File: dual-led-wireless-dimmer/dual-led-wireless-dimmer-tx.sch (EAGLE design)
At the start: 43 parts, among them IC1 LM2937IMP-3.3, Q1 DN2625K4-G, Q2 SI2323DS-T1-E3, Q3 IRF520NPBF, Q4 IRF520NPBF, U1 ATMEGA328P_TQFP

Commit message: wip
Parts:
- added R12, R13: 150, microbuilder:RESISTOR0805
- Q3, Q4: value IRF520NPBF -> IRL520
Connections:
- new net N$1: Q3.G, R12.2
- new net N$2: Q4.G, R13.2
- net PWM1: now also R12.1; no longer Q3.G
- net PWM2: now also R13.1; no longer Q4.G
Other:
- moved on the sheet: OUT1-1, OUT1-2, OUT2-1, OUT2-2, Q3, Q4
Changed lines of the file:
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@@
 <?xml version="1.0" encoding="utf-8"?>
 <!DOCTYPE eagle SYSTEM "eagle.dtd">
-<eagle version="8.5.0">
+<eagle version="8.5.1">
 <drawing>
 <settings>
@@
 <part name="3.3V7" library="microbuilder" deviceset="3.3V" device=""/>
 <part name="12V1" library="microbuilder" deviceset="12V" device=""/>
-<part name="Q3" library="Seeed-Transistor-2016" deviceset="DIP-MOSFET-N-CH-100V-9.7A-IRF520NPBF(TO-220AB)" device="" value="IRF520NPBF"/>
+<part name="Q3" library="Seeed-Transistor-2016" deviceset="DIP-MOSFET-N-CH-100V-9.7A-IRF520NPBF(TO-220AB)" device="" value="IRL520"/>
 <part name="OUT1" library="con-ptr500" library_urn="urn:adsk.eagle:library:181" deviceset="AK550/2" device="" package3d_urn="urn:adsk.eagle:package:9907/1"/>
 <part name="12V2" library="microbuilder" deviceset="12V" device=""/>
@@
 <part name="R10" library="microbuilder" deviceset="RESISTOR" device="0805" value="10k"/>
 <part name="GND16" library="microbuilder" deviceset="GND" device=""/>
-<part name="Q4" library="Seeed-Transistor-2016" deviceset="DIP-MOSFET-N-CH-100V-9.7A-IRF520NPBF(TO-220AB)" device="" value="IRF520NPBF"/>
+<part name="Q4" library="Seeed-Transistor-2016" deviceset="DIP-MOSFET-N-CH-100V-9.7A-IRF520NPBF(TO-220AB)" device="" value="IRL520"/>
 <part name="OUT2" library="con-ptr500" library_urn="urn:adsk.eagle:library:181" deviceset="AK550/2" device="" package3d_urn="urn:adsk.eagle:package:9907/1"/>
 <part name="12V3" library="microbuilder" deviceset="12V" device=""/>
@@
 <part name="SJ3" library="SparkFun-Retired" deviceset="SOLDERJUMPER" device="NO"/>
 <part name="SJ1" library="SparkFun-Retired" deviceset="SOLDERJUMPER" device="NO"/>
+<part name="R12" library="microbuilder" deviceset="RESISTOR" device="0805" value="150"/>
+<part name="R13" library="microbuilder" deviceset="RESISTOR" device="0805" value="150"/>
 </parts>
 <sheets>
@@
 <instance part="3.3V7" gate="G$1" x="149.86" y="137.16" rot="R180"/>
 <instance part="12V1" gate="G$1" x="91.44" y="10.16"/>
-<instance part="Q3" gate="G$1" x="248.92" y="99.06"/>
-<instance part="OUT1" gate="-1" x="254" y="106.68" rot="R180"/>
-<instance part="OUT1" gate="-2" x="254" y="111.76" rot="R180"/>
-<instance part="12V2" gate="G$1" x="248.92" y="119.38"/>
-<instance part="GND18" gate="G$1" x="248.92" y="88.9"/>
+<instance part="Q3" gate="G$1" x="266.7" y="99.06"/>
+<instance part="OUT1" gate="-1" x="271.78" y="106.68" rot="R180"/>
+<instance part="OUT1" gate="-2" x="271.78" y="111.76" rot="R180"/>
+<instance part="12V2" gate="G$1" x="266.7" y="119.38"/>
+<instance part="GND18" gate="G$1" x="266.7" y="88.9"/>
 <instance part="R10" gate="G$1" x="238.76" y="93.98" rot="R270"/>
 <instance part="GND16" gate="G$1" x="238.76" y="86.36"/>
-<instance part="Q4" gate="G$1" x="248.92" y="60.96"/>
-<instance part="OUT2" gate="-1" x="254" y="68.58" rot="R180"/>
-<instance part="OUT2" gate="-2" x="254" y="73.66" rot="R180"/>
-<instance part="12V3" gate="G$1" x="248.92" y="81.28"/>
-<instance part="GND19" gate="G$1" x="248.92" y="50.8"/>
+<instance part="Q4" gate="G$1" x="266.7" y="60.96"/>
+<instance part="OUT2" gate="-1" x="271.78" y="68.58" rot="R180"/>
+<instance part="OUT2" gate="-2" x="271.78" y="73.66" rot="R180"/>
+<instance part="12V3" gate="G$1" x="266.7" y="81.28"/>
+<instance part="GND19" gate="G$1" x="266.7" y="50.8"/>
 <instance part="R11" gate="G$1" x="238.76" y="55.88" rot="R270"/>
 <instance part="GND17" gate="G$1" x="238.76" y="48.26"/>
@@
 <instance part="SJ3" gate="1" x="198.12" y="111.76"/>
 <instance part="SJ1" gate="1" x="198.12" y="116.84"/>
+<instance part="R12" gate="G$1" x="251.46" y="99.06"/>
+<instance part="R13" gate="G$1" x="251.46" y="60.96"/>
 </instances>
 <busses>
@@
 <pinref part="Q3" gate="G$1" pin="S"/>
 <pinref part="GND18" gate="G$1" pin="GND"/>
-<wire x1="248.92" y1="91.44" x2="248.92" y2="93.98" width="0.1524" layer="91"/>
+<wire x1="266.7" y1="91.44" x2="266.7" y2="93.98" width="0.1524" layer="91"/>
 </segment>
 <segment>
@@
 <pinref part="Q4" gate="G$1" pin="S"/>
 <pinref part="GND19" gate="G$1" pin="GND"/>
-<wire x1="248.92" y1="53.34" x2="248.92" y2="55.88" width="0.1524" layer="91"/>
+<wire x1="266.7" y1="53.34" x2="266.7" y2="55.88" width="0.1524" layer="91"/>
 </segment>
 <segment>
@@
 <segment>
 <pinref part="12V2" gate="G$1" pin="12V"/>
-<wire x1="248.92" y1="116.84" x2="248.92" y2="111.76" width="0.1524" layer="91"/>
+<wire x1="266.7" y1="116.84" x2="266.7" y2="111.76" width="0.1524" layer="91"/>
 <pinref part="OUT1" gate="-2" pin="KL"/>
 </segment>
 <segment>
 <pinref part="12V3" gate="G$1" pin="12V"/>
-<wire x1="248.92" y1="78.74" x2="248.92" y2="73.66" width="0.1524" layer="91"/>
+<wire x1="266.7" y1="78.74" x2="266.7" y2="73.66" width="0.1524" layer="91"/>
 <pinref part="OUT2" gate="-2" pin="KL"/>
 </segment>
@@
 <pinref part="OUT1" gate="-1" pin="KL"/>
 <pinref part="Q3" gate="G$1" pin="D"/>
-<wire x1="248.92" y1="106.68" x2="248.92" y2="104.14" width="0.1524" layer="91"/>
+<wire x1="266.7" y1="106.68" x2="266.7" y2="104.14" width="0.1524" layer="91"/>
 </segment>
 </net>
 <net name="PWM1" class="0">
 <segment>
-<pinref part="Q3" gate="G$1" pin="G"/>
-<wire x1="243.84" y1="99.06" x2="238.76" y2="99.06" width="0.1524" layer="91"/>
 <pinref part="R10" gate="G$1" pin="1"/>
 <wire x1="238.76" y1="99.06" x2="233.68" y2="99.06" width="0.1524" layer="91"/>
+<label x="228.6" y="99.06" size="1.778" layer="95"/>
+<pinref part="R12" gate="G$1" pin="1"/>
+<wire x1="238.76" y1="99.06" x2="246.38" y2="99.06" width="0.1524" layer="91"/>
 <junction x="238.76" y="99.06"/>
-<label x="228.6" y="99.06" size="1.778" layer="95"/>
 </segment>
 <segment>
@@
 <pinref part="OUT2" gate="-1" pin="KL"/>
 <pinref part="Q4" gate="G$1" pin="D"/>
-<wire x1="248.92" y1="68.58" x2="248.92" y2="66.04" width="0.1524" layer="91"/>
+<wire x1="266.7" y1="68.58" x2="266.7" y2="66.04" width="0.1524" layer="91"/>
 </segment>
 </net>
 <net name="PWM2" class="0">
 <segment>
-<pinref part="Q4" gate="G$1" pin="G"/>
-<wire x1="243.84" y1="60.96" x2="238.76" y2="60.96" width="0.1524" layer="91"/>
 <pinref part="R11" gate="G$1" pin="1"/>
 <wire x1="238.76" y1="60.96" x2="233.68" y2="60.96" width="0.1524" layer="91"/>
+<label x="228.6" y="60.96" size="1.778" layer="95"/>
+<pinref part="R13" gate="G$1" pin="1"/>
+<wire x1="246.38" y1="60.96" x2="238.76" y2="60.96" width="0.1524" layer="91"/>
 <junction x="238.76" y="60.96"/>
-<label x="228.6" y="60.96" size="1.778" layer="95"/>
 </segment>
 <segment>
@@
 </segment>
 </net>
+<net name="N$1" class="0">
+<segment>
+<pinref part="Q3" gate="G$1" pin="G"/>
+<pinref part="R12" gate="G$1" pin="2"/>
+<wire x1="256.54" y1="99.06" x2="261.62" y2="99.06" width="0.1524" layer="91"/>
+</segment>
+</net>
+<net name="N$2" class="0">
+<segment>
+<pinref part="Q4" gate="G$1" pin="G"/>
+<pinref part="R13" gate="G$1" pin="2"/>
+<wire x1="256.54" y1="60.96" x2="261.62" y2="60.96" width="0.1524" layer="91"/>
+</segment>
+</net>

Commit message: wip
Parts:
- CH1: SPICEPREFIX (none) -> C
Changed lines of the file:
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@@
 </classes>
 <parts>
-<part name="CH1" library="keves-ng" deviceset="PTL45" device=""/>
-<part name="CH2" library="keves-ng" deviceset="PTL45" device=""/>
+<part name="CH1" library="keves-ng" library_urn="urn:adsk.eagle:library:1429743" deviceset="PTL45" device="" package3d_urn="urn:adsk.eagle:package:1429786/2">
+<attribute name="SPICEPREFIX" value="C"/>
+</part>
+<part name="CH2" library="keves-ng" library_urn="urn:adsk.eagle:library:1429743" deviceset="PTL45" device="" package3d_urn="urn:adsk.eagle:package:1429786/2"/>
 <part name="U1" library="SparkFun-DigitalIC" deviceset="ATMEGA328P_TQFP" device="" value="ATMEGA328P_TQFP"/>
 <part name="GND9" library="microbuilder" deviceset="GND" device=""/>
@@
 <part name="R9" library="microbuilder" deviceset="RESISTOR" device="0805" value="220"/>
 <part name="R8" library="microbuilder" deviceset="RESISTOR" device="0805" value="220"/>
-<part name="F1" library="keves-ng" deviceset="KEYSTONE-3557-2" device=""/>
+<part name="F1" library="keves-ng" library_urn="urn:adsk.eagle:library:1429743" deviceset="KEYSTONE-3557-2" device="" package3d_urn="urn:adsk.eagle:package:1429787/2"/>
 <part name="Q1" library="SparkFun-DiscreteSemi" deviceset="MOSFET-NCHANNEL" device="FDD8780" value="DN2625K4-G"/>
 <part name="R3" library="microbuilder" deviceset="RESISTOR" device="0805" value="100k"/>

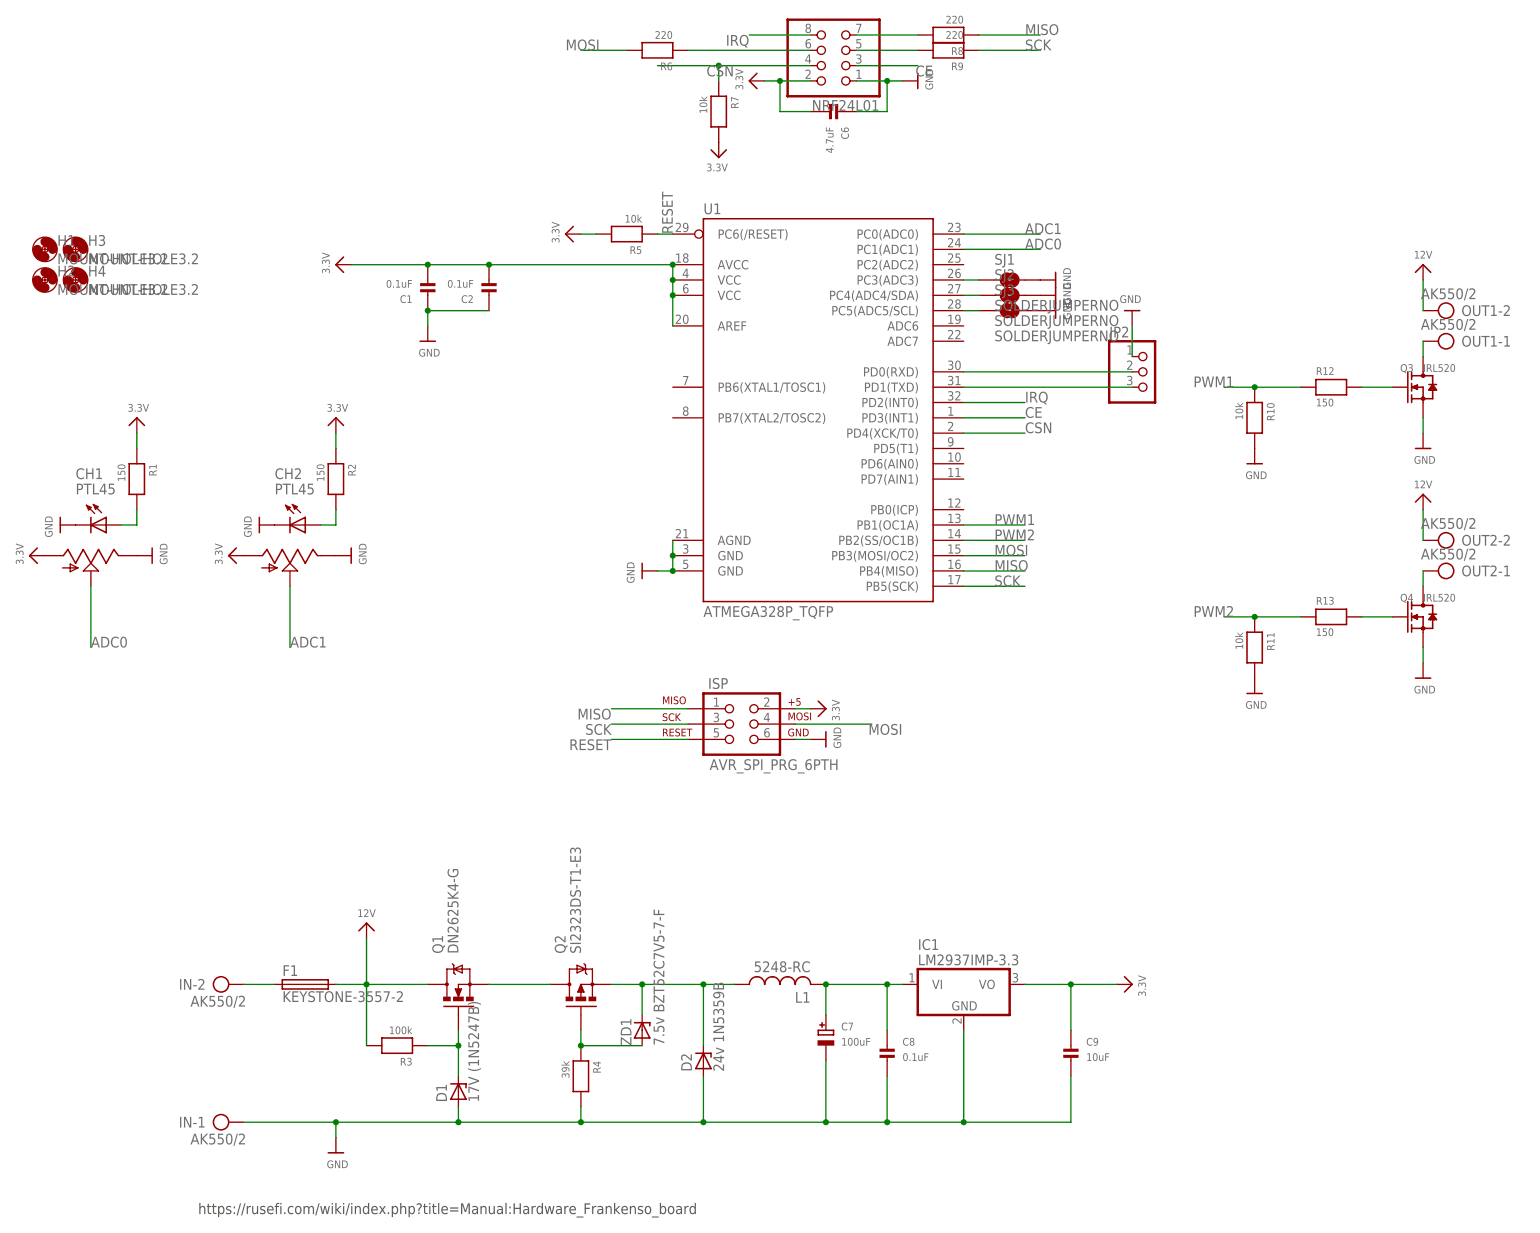
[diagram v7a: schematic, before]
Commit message: dual led wireless dimmer rev 2
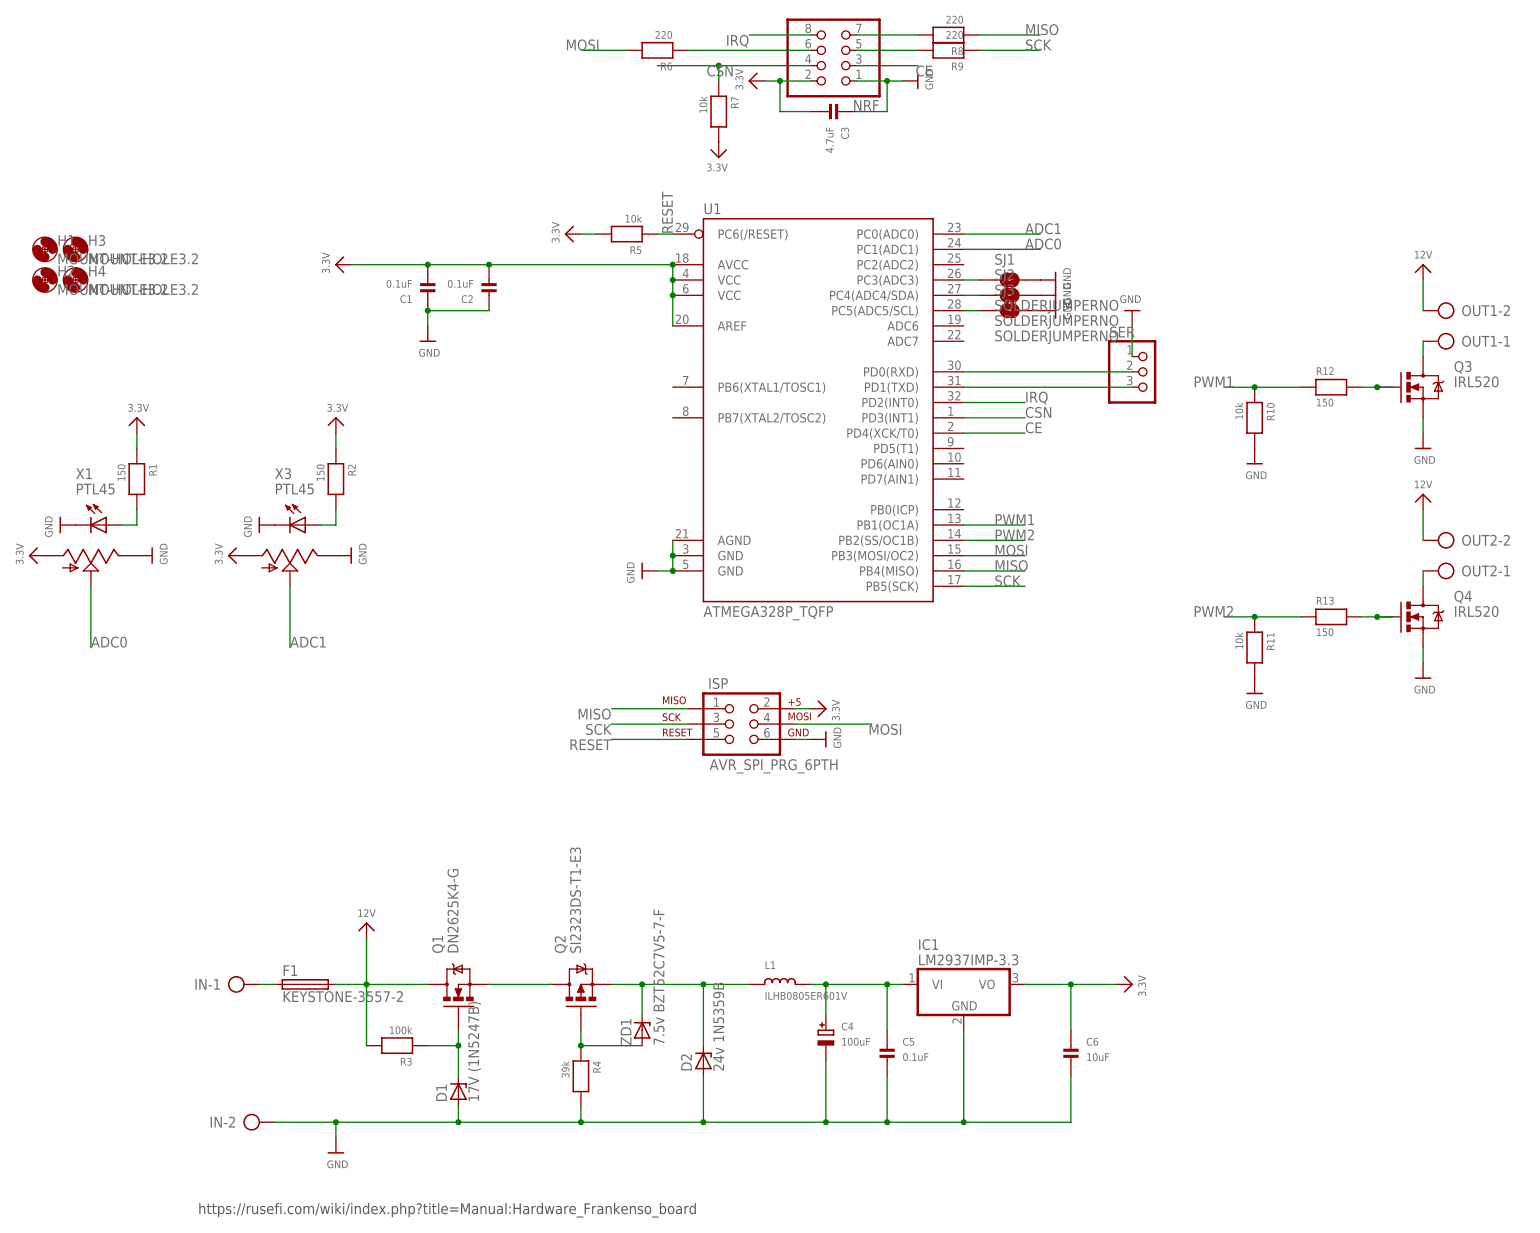
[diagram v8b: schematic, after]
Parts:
- removed C9: 10uF, microbuilder:CAP_CERAMIC0805
- added C3: 4.7uF, microbuilder:CAP_CERAMIC0805
- C6: value 4.7uF -> 10uF
- D2: device diode:ZENER-DIODEZD-10 -> diode:ZPY
- IN, OUT1, OUT2: value AK550/2 -> (none); device con-ptr500:AK550/2 -> con-ptr500:AK500/2-H
- L1: value 5248-RC -> ILHB0805ER601V; device rcl:L-US0207/5V -> microbuilder:INDUCTOR0805
- Q3, Q4: device Seeed-Transistor-2016:DIP-MOSFET-N-CH-100V-9.7A-IRF520NPBF(TO-220AB) -> keves-ng:MOSFET-NCHANNELFQP30N06L
- renumbered C7 to C4, C8 to C5, CH1 to X1, CH2 to X3, JP2 to SER, NRF24L01 to NRF
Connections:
- net JP1 renamed N$66
- net 3.3V: now also C3.P$2, C6.P$1; no longer C6.P$2, C9.P$1
- net CE: now also U1.PD4(XCK/T0); no longer U1.PD3(INT1)
- net CSN: now also U1.PD3(INT1); no longer U1.PD4(XCK/T0)
- net GND: now also C3.P$1, C6.P$2, IN-2.KL; no longer C6.P$1, C9.P$2, IN-1.KL
- net N$5: now also IN-1.KL; no longer IN-2.KL
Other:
- moved on the sheet: C6, IN-1, IN-2
